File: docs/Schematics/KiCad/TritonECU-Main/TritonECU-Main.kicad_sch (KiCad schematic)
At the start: 0 parts

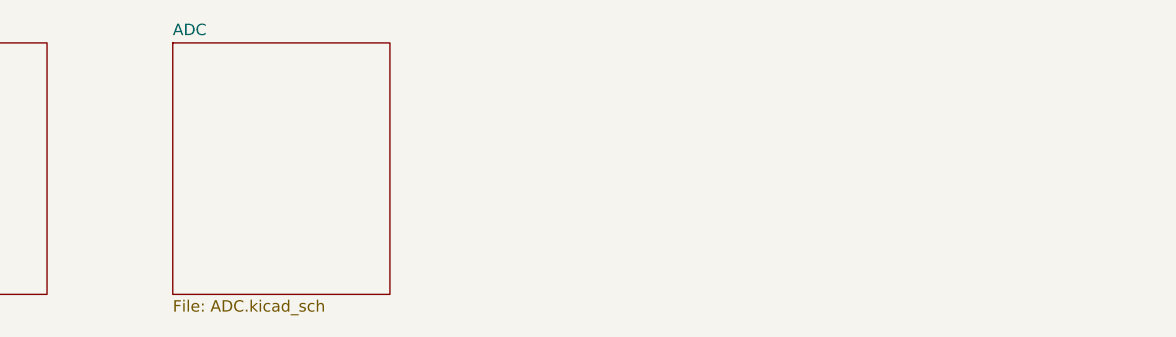
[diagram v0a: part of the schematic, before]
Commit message: Carrier: ignition, injection and rails sheets, placed on the main board
- eecv_pins.py: the EEC-V connector map for the 5.4L, checked. Corrects SSA/SSB
  to pins 6/11: Ford's "PCM 27 (*6)" legend is * = 5.4L, and 27/1 are coils 5/6
  on this truck (schematic-ecu-v1.txt and measurements-wanted.md fixed).
- carrier_pinmap.py: adds TCS (O/D cancel, pin 29) on PE1, polled; 4x4-low has
  no PCM pin in either source, marked [CONFIRM]. 100 signals, 5 spare.
- Interconnect sheet rebuilt every run with every connector and module pin
  labelled from the two maps (symbol UUIDs kept); deliberate no-connects flagged.
- gen_carrier.py: Rails, Ignition (74HCT541, 8x ISL9V3040, TPS3823A-33 watchdog
  on NRST and OE2 via BSS138, JP101 v1 strap) and Injection (8x ZXMS6005DGQ,
  10k input pulldowns). Deterministic symbol UUIDs keep the PCB linked. Own
  symbols for the IntelliFET (the Samacsys import is broken) and NCV8772.
- gen_carrier_pcb.py: adds missing parts to the board linked to their symbols,
  sets every pad net from the netlist, places a first-draft floor plan by
  connector position. DRC: no courtyard overlaps, schematic parity clean.
- ADC goes back on the carrier: adc-daughterboard.md superseded.

Co-Authored-By: Claude Opus 5.5 <noreply@anthropic.com>
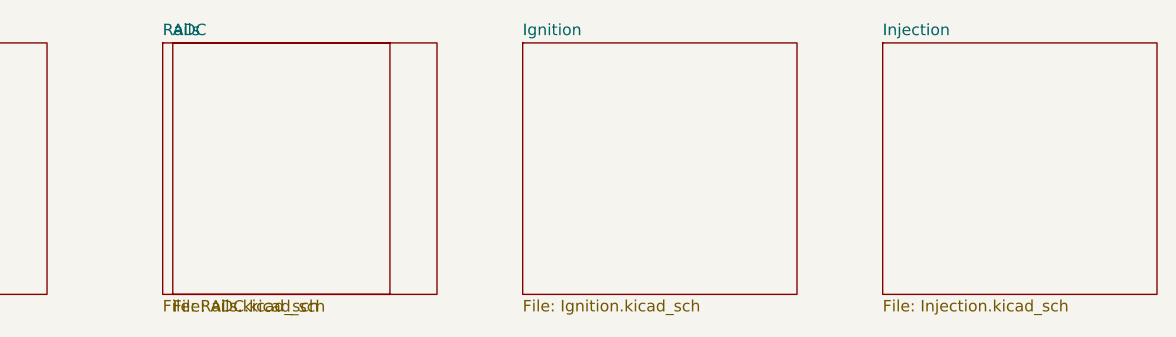
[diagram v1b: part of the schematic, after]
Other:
- added sheet Ignition (Ignition.kicad_sch)
- added sheet Injection (Injection.kicad_sch)
- added sheet Rails (Rails.kicad_sch)
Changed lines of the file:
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@@
 		(instances (project "TritonECU-Main" (path "/eec527cb-b372-4ed4-ac2b-16ccf6980056" (page "3"))))
+	)
+	(sheet (at 70 30.48) (size 30.48 27.94) (exclude_from_sim no) (in_bom yes) (on_board yes) (dnp no)
+		(stroke (width 0.1524) (type solid)) (fill (color 0 0 0 0))
+		(property "Sheetname" "Rails" (at 70 29.77 0) (effects (font (size 1.27 1.27)) (justify left bottom)))
+		(property "Sheetfile" "Rails.kicad_sch" (at 70 58.980000000000004 0) (effects (font (size 1.27 1.27)) (justify left top)))
+		(instances (project "TritonECU-Main" (path "/eec527cb-b372-4ed4-ac2b-16ccf6980056" (page "4"))))
+	)
+	(sheet (at 110 30.48) (size 30.48 27.94) (exclude_from_sim no) (in_bom yes) (on_board yes) (dnp no)
+		(stroke (width 0.1524) (type solid)) (fill (color 0 0 0 0))
+		(property "Sheetname" "Ignition" (at 110 29.77 0) (effects (font (size 1.27 1.27)) (justify left bottom)))
+		(property "Sheetfile" "Ignition.kicad_sch" (at 110 58.980000000000004 0) (effects (font (size 1.27 1.27)) (justify left top)))
+		(instances (project "TritonECU-Main" (path "/eec527cb-b372-4ed4-ac2b-16ccf6980056" (page "5"))))
+	)
+	(sheet (at 150 30.48) (size 30.48 27.94) (exclude_from_sim no) (in_bom yes) (on_board yes) (dnp no)
+		(stroke (width 0.1524) (type solid)) (fill (color 0 0 0 0))
+		(property "Sheetname" "Injection" (at 150 29.77 0) (effects (font (size 1.27 1.27)) (justify left bottom)))
+		(property "Sheetfile" "Injection.kicad_sch" (at 150 58.980000000000004 0) (effects (font (size 1.27 1.27)) (justify left top)))
+		(instances (project "TritonECU-Main" (path "/eec527cb-b372-4ed4-ac2b-16ccf6980056" (page "6"))))
 	)
 	(sheet_instances

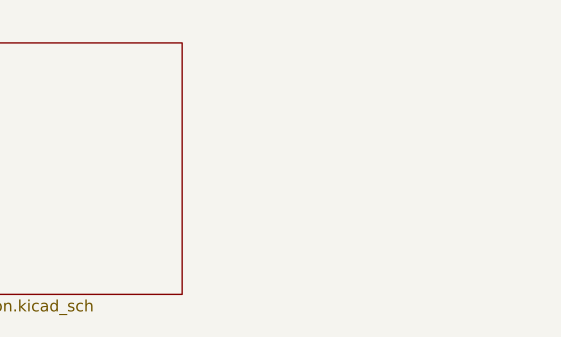
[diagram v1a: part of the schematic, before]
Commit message: Carrier: VR front end on the main board, 3 x MAX9926
The VR daughterboard (DB2) is removed; the conditioning moves onto the carrier
as Vr.kicad_sch, U301-U303: CKP + spare, CMP + OSS, TSS + transfer case. All
V1 review fixes applied: 2 x 5k 0805 per input leg (300 V), 470 pF C0G 200 V
across the inputs, 100 nF on BIAS, 10n + 100n + 1u per VCC. Single-ended
sensors return on SIGRTN; the CMP shield goes single-point to the star through
R399; the spare channel is on header J301. VR board V1 stays the bench board.

Placed where DB2 was, under the CMP/OSS/TSS/TC pins. ERC 0 errors, PCB
schematic parity clean, no courtyard overlaps.

Generators: lock check ignores the project window alone; stale footprints are
removed after the new ones load (a Remove first broke the footprint loader).

Co-Authored-By: Claude Opus 5.5 <noreply@anthropic.com>
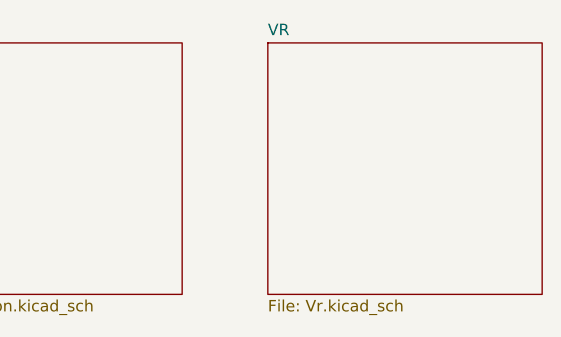
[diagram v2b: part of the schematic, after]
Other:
- added sheet VR (Vr.kicad_sch)
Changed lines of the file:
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@@
 		(instances (project "TritonECU-Main" (path "/eec527cb-b372-4ed4-ac2b-16ccf6980056" (page "6"))))
+	)
+	(sheet (at 190 30.48) (size 30.48 27.94) (exclude_from_sim no) (in_bom yes) (on_board yes) (dnp no)
+		(stroke (width 0.1524) (type solid)) (fill (color 0 0 0 0))
+		(property "Sheetname" "VR" (at 190 29.77 0) (effects (font (size 1.27 1.27)) (justify left bottom)))
+		(property "Sheetfile" "Vr.kicad_sch" (at 190 58.980000000000004 0) (effects (font (size 1.27 1.27)) (justify left top)))
+		(instances (project "TritonECU-Main" (path "/eec527cb-b372-4ed4-ac2b-16ccf6980056" (page "7"))))
 	)
 	(sheet_instances

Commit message: Carrier: Solenoids and PWM sheets, placed on the main board
Solenoids: NCV8405A low-side drivers for the HO2S heaters, vent, IMCC,
SSA/SSB, with 74HCT541 buffering and a 74HC4051 mux for output-sense
dividers. PWM: EVAP, EGR, TCC, EPC, IAC, VSS out, CCS with freewheel
Schottkys (part [CONFIRM]) and supply-sense dividers. ERC 0 errors,
DRC 0 parity issues.

Co-Authored-By: Claude Opus 5.5 <noreply@anthropic.com>
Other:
- added sheet PWM (Pwm.kicad_sch)
- added sheet Solenoids (Solenoids.kicad_sch)
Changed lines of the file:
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@@
 		(instances (project "TritonECU-Main" (path "/eec527cb-b372-4ed4-ac2b-16ccf6980056" (page "7"))))
+	)
+	(sheet (at 70 70.48) (size 30.48 27.94) (exclude_from_sim no) (in_bom yes) (on_board yes) (dnp no)
+		(stroke (width 0.1524) (type solid)) (fill (color 0 0 0 0))
+		(property "Sheetname" "Solenoids" (at 70 69.77000000000001 0) (effects (font (size 1.27 1.27)) (justify left bottom)))
+		(property "Sheetfile" "Solenoids.kicad_sch" (at 70 98.98 0) (effects (font (size 1.27 1.27)) (justify left top)))
+		(instances (project "TritonECU-Main" (path "/eec527cb-b372-4ed4-ac2b-16ccf6980056" (page "8"))))
+	)
+	(sheet (at 110 70.48) (size 30.48 27.94) (exclude_from_sim no) (in_bom yes) (on_board yes) (dnp no)
+		(stroke (width 0.1524) (type solid)) (fill (color 0 0 0 0))
+		(property "Sheetname" "PWM" (at 110 69.77000000000001 0) (effects (font (size 1.27 1.27)) (justify left bottom)))
+		(property "Sheetfile" "Pwm.kicad_sch" (at 110 98.98 0) (effects (font (size 1.27 1.27)) (justify left top)))
+		(instances (project "TritonECU-Main" (path "/eec527cb-b372-4ed4-ac2b-16ccf6980056" (page "9"))))
 	)
 	(sheet_instances

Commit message: Carrier: Relays sheet (TBD62083AFNG), placed on the main board
FPUMP, FAN1, FAN2, ACC straight from GPIO with 100k pulldowns; PTC per
output (the array has no current limit); COMMON on permanent B+ (pin 55,
[CONFIRM] sharing with the battery-sense divider). Channels 5-8 spare.

Co-Authored-By: Claude Opus 5.5 <noreply@anthropic.com>
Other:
- added sheet Relays (Relays.kicad_sch)
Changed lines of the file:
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@@
 		(instances (project "TritonECU-Main" (path "/eec527cb-b372-4ed4-ac2b-16ccf6980056" (page "9"))))
+	)
+	(sheet (at 150 70.48) (size 30.48 27.94) (exclude_from_sim no) (in_bom yes) (on_board yes) (dnp no)
+		(stroke (width 0.1524) (type solid)) (fill (color 0 0 0 0))
+		(property "Sheetname" "Relays" (at 150 69.77000000000001 0) (effects (font (size 1.27 1.27)) (justify left bottom)))
+		(property "Sheetfile" "Relays.kicad_sch" (at 150 98.98 0) (effects (font (size 1.27 1.27)) (justify left top)))
+		(instances (project "TritonECU-Main" (path "/eec527cb-b372-4ed4-ac2b-16ccf6980056" (page "10"))))
 	)
 	(sheet_instances

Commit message: Carrier: VREF sheet, and the power board's +VIN is VPROT, not VPWR
VREF: NCV8772C 5.00 V on the protected rail, EN from the MCU; TPS2H160B-Q1
at 248 mA per feed, latch mode; LM74700-Q1 + DMN6040 ideal diode and
SMAJ24CA per feed; 100k/12.4k short-to-battery sense. Channel 2 drawn,
not fitted (one VREF pin, 90).

Fix: power board J3 +VIN is the LTC4364 OUTPUT (IC1 pin 1, after R2).
The carrier had it on VPWR, joining the surge stopper's output to its
raw input. It is now its own net, VPROT, which also feeds VREF.

gen_carrier_pcb.py: no-connect pins get their unconnected net (parity),
and --replace-sheet NAME re-places one sheet's parts.

Co-Authored-By: Claude Opus 5.5 <noreply@anthropic.com>
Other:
- added sheet VREF (Vref.kicad_sch)
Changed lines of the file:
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@@
 		(instances (project "TritonECU-Main" (path "/eec527cb-b372-4ed4-ac2b-16ccf6980056" (page "10"))))
+	)
+	(sheet (at 190 70.48) (size 30.48 27.94) (exclude_from_sim no) (in_bom yes) (on_board yes) (dnp no)
+		(stroke (width 0.1524) (type solid)) (fill (color 0 0 0 0))
+		(property "Sheetname" "VREF" (at 190 69.77000000000001 0) (effects (font (size 1.27 1.27)) (justify left bottom)))
+		(property "Sheetfile" "Vref.kicad_sch" (at 190 98.98 0) (effects (font (size 1.27 1.27)) (justify left top)))
+		(instances (project "TritonECU-Main" (path "/eec527cb-b372-4ed4-ac2b-16ccf6980056" (page "11"))))
 	)
 	(sheet_instances

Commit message: Carrier: Comms sheet (SCP, CAN, USB-C, microSD)
SCP: DRV8837 (coast = passive, nSLEEP 10k low), 100R per line, NUP2105L;
TLV7031 RX with the corrected 100k:100k divider to GND, MM3Z3V3 clamps,
4.7M hysteresis, 100R + SMF3.3A out. CAN: TJA1042T/3, RXD also to PA0
WKUP1, split termination 2 x 60.4R + 4.7n, NUP2105L; bus on EEC-V 42/43
(added terminals, unused cavities). USB-C device (USB4105, 5.1k CC,
USBLC6-2SC6, VBUS sense). microSD Molex 104031 on SDMMC2 1-bit, powered
through a TPS22917 on SD_PWR_EN (PG11): 3.3 V is always on.

USB-C on the right board edge; microSD parked off-board (wider than the
free strip). Scoped DRC rule for the USB4105 land pattern.

Co-Authored-By: Claude Opus 5.5 <noreply@anthropic.com>
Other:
- added sheet Comms (Comms.kicad_sch)
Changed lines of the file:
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@@
 		(instances (project "TritonECU-Main" (path "/eec527cb-b372-4ed4-ac2b-16ccf6980056" (page "11"))))
+	)
+	(sheet (at 110 110.48) (size 30.48 27.94) (exclude_from_sim no) (in_bom yes) (on_board yes) (dnp no)
+		(stroke (width 0.1524) (type solid)) (fill (color 0 0 0 0))
+		(property "Sheetname" "Comms" (at 110 109.77000000000001 0) (effects (font (size 1.27 1.27)) (justify left bottom)))
+		(property "Sheetfile" "Comms.kicad_sch" (at 110 138.98000000000002 0) (effects (font (size 1.27 1.27)) (justify left top)))
+		(instances (project "TritonECU-Main" (path "/eec527cb-b372-4ed4-ac2b-16ccf6980056" (page "13"))))
 	)
 	(sheet_instances

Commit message: Carrier: Inputs sheet and switched rails for sleep
Inputs: one network per switch input - 4.7k pull-up to VPWR (ground-
switched only; VPWR so a TR bit closed in Park draws nothing parked),
SMF24A, 33k/15k, 10n, BAT54J to 3.3 V. TR1/2/4 and 4X4L ground-switched,
TR3A/BRAKE/ACP/TCS 12 V high-side. 4X4L mapped to EEC-V pin 14
(findings sec.14). IGN_WAKE from VPWR into PC13/WKUP4. TACH/SPEED bench
header, BOOT0 DFU solder jumper.

Switched rails: +5V and +3.3V stay up parked, so two TPS22917 load
switches on SW_RAIL_EN (PG12, 100k down) make +5V_SW / +3.3V_SW for the
running-only loads: 74HCT541 x3 and OE pull-ups, MAX9926 x3 and COUT
pull-ups, ADS8588H, OPA2376 x2, O2 bias, knock block, 74HC4051, TPS2H160B
FAULT pull-up, TFT pull-up. MCU, watchdog, CAN, SCP RX, clamps stay on.

gen_carrier_pcb.py: packer steps around existing parts, fills several
rects in turn, parks overflow below earlier parked parts.

Co-Authored-By: Claude Opus 5.5 <noreply@anthropic.com>
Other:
- added sheet Inputs (Inputs.kicad_sch)
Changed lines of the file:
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@@
 		(instances (project "TritonECU-Main" (path "/eec527cb-b372-4ed4-ac2b-16ccf6980056" (page "13"))))
+	)
+	(sheet (at 150 110.48) (size 30.48 27.94) (exclude_from_sim no) (in_bom yes) (on_board yes) (dnp no)
+		(stroke (width 0.1524) (type solid)) (fill (color 0 0 0 0))
+		(property "Sheetname" "Inputs" (at 150 109.77000000000001 0) (effects (font (size 1.27 1.27)) (justify left bottom)))
+		(property "Sheetfile" "Inputs.kicad_sch" (at 150 138.98000000000002 0) (effects (font (size 1.27 1.27)) (justify left top)))
+		(instances (project "TritonECU-Main" (path "/eec527cb-b372-4ed4-ac2b-16ccf6980056" (page "14"))))
 	)
 	(sheet_instances
